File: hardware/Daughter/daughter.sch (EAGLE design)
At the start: 4 parts, among them J1 12V input

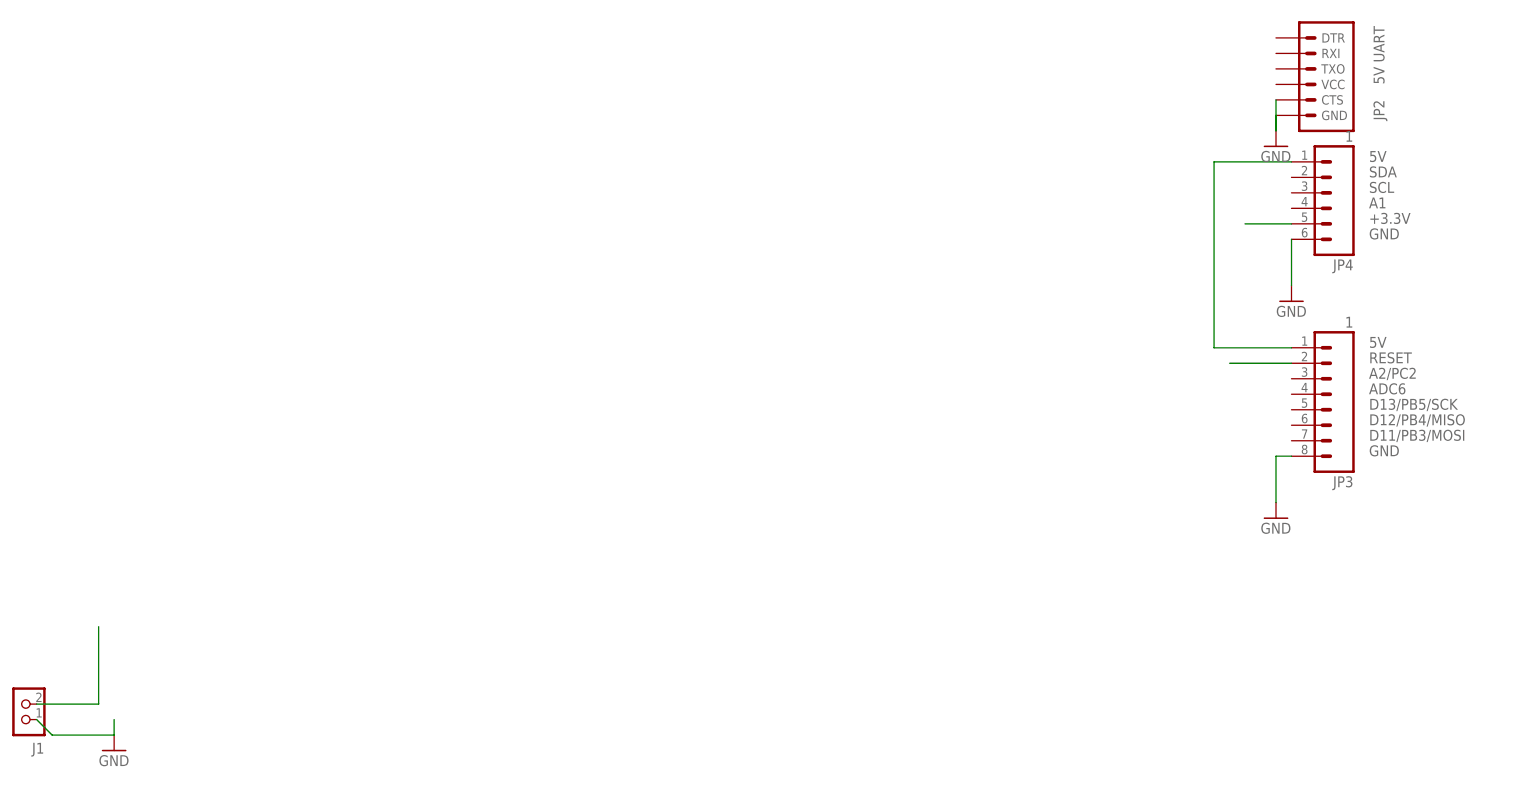
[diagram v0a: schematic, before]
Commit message: added 12_adc_daughter/LTC2495_16x_pga_adc.pdf removed eagle.epf files and added gitignore file
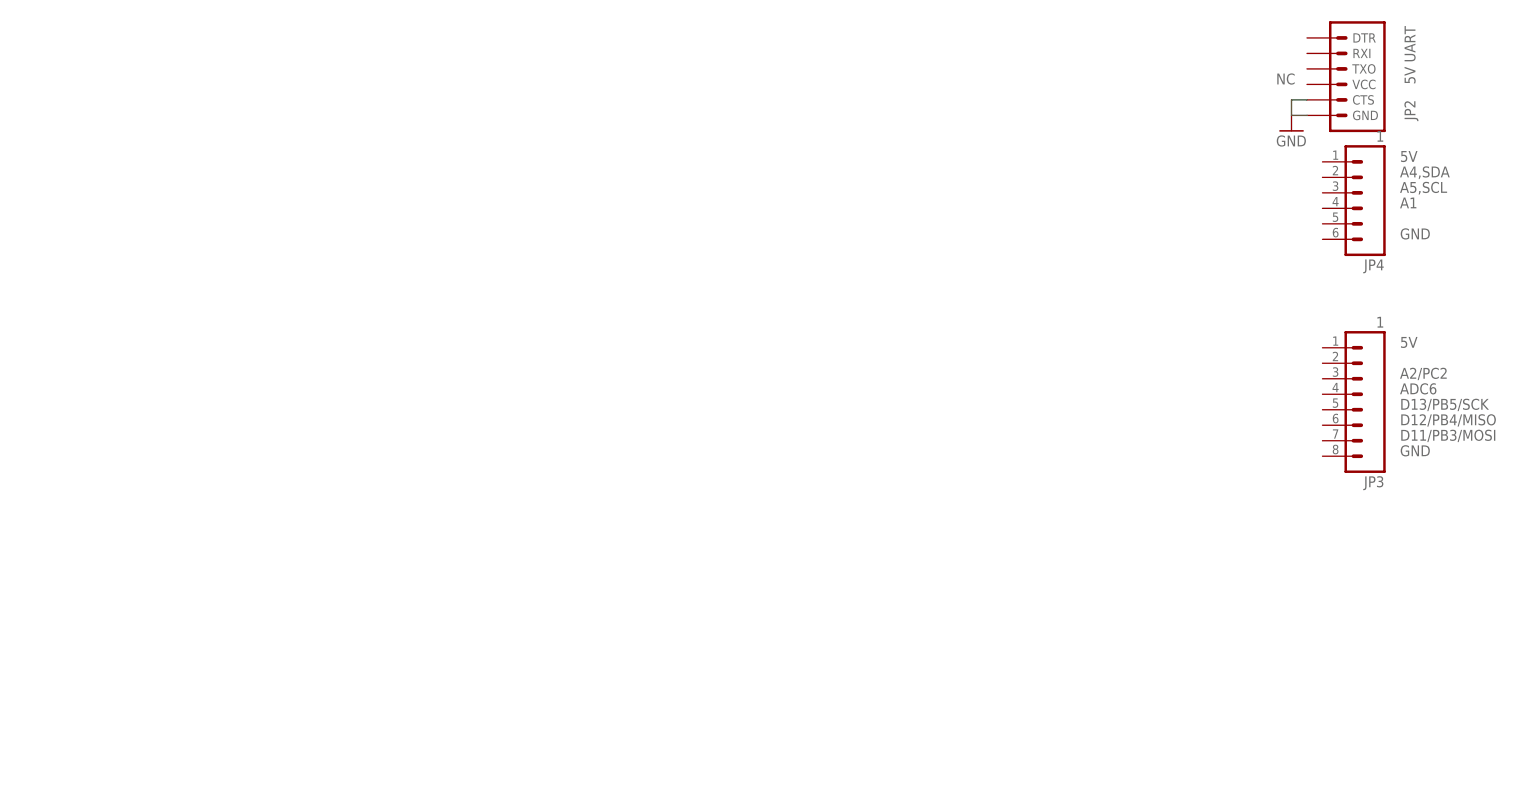
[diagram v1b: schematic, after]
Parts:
- removed J1: 12V input, dp_devices:CON_HEADER_1X02-PTH
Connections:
- removed net +12V: J1.2
- removed net +3.3V: JP4.5
- removed net +5V: JP3.1, JP4.1
- removed net RESET: JP3.2
- net GND: no longer J1.1, JP3.8, JP4.6
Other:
- note added: "A4,SDA"
- note added: "A5,SCL"
- note added: "NC"
- note removed: "SCL"
- note removed: "SDA"
- moved on the sheet: JP2, JP3, JP4
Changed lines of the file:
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@@
 </classes>
 <parts>
-<part name="J1" library="dp_devices" deviceset="CON_HEADER_1X02" device="-PTH" value="12V input"/>
-<part name="GND32" library="SparkFun" deviceset="GND" device=""/>
 <part name="JP2" library="SparkFun" deviceset="ARDUINO_SERIAL_PROGRAM" device="PTH" value="5V UART"/>
 <part name="GND3" library="SparkFun" deviceset="GND" device=""/>
 <part name="JP4" library="SparkFun-Connectors" deviceset="M06" device="SIP" value="1"/>
-<part name="GND5" library="SparkFun" deviceset="GND" device=""/>
-<part name="GND6" library="SparkFun" deviceset="GND" device=""/>
 <part name="JP3" library="SparkFun-Connectors" deviceset="M08" device="1X08" value="1"/>
 </parts>
@@
 <sheet>
 <plain>
-<text x="213.36" y="190.5" size="1.778" layer="95">SDA</text>
-<text x="213.36" y="187.96" size="1.778" layer="95">SCL</text>
-<text x="213.36" y="185.42" size="1.778" layer="95">A1</text>
-<text x="213.36" y="193.04" size="1.778" layer="95">5V</text>
-<text x="213.36" y="162.56" size="1.778" layer="95">5V</text>
-<text x="213.36" y="144.78" size="1.778" layer="95">GND</text>
-<text x="213.36" y="180.34" size="1.778" layer="95">GND</text>
-<text x="213.36" y="157.48" size="1.778" layer="95">A2/PC2</text>
-<text x="213.36" y="154.94" size="1.778" layer="95">ADC6</text>
-<text x="213.36" y="152.4" size="1.778" layer="95">D13/PB5/SCK</text>
-<text x="213.36" y="149.86" size="1.778" layer="95">D12/PB4/MISO</text>
-<text x="213.36" y="147.32" size="1.778" layer="95">D11/PB3/MOSI</text>
+<text x="218.44" y="190.5" size="1.778" layer="95">A4,SDA</text>
+<text x="218.44" y="187.96" size="1.778" layer="95">A5,SCL</text>
+<text x="218.44" y="185.42" size="1.778" layer="95">A1</text>
+<text x="218.44" y="193.04" size="1.778" layer="95">5V</text>
+<text x="218.44" y="162.56" size="1.778" layer="95">5V</text>
+<text x="218.44" y="144.78" size="1.778" layer="95">GND</text>
+<text x="218.44" y="180.34" size="1.778" layer="95">GND</text>
+<text x="218.44" y="157.48" size="1.778" layer="95">A2/PC2</text>
+<text x="218.44" y="154.94" size="1.778" layer="95">ADC6</text>
+<text x="218.44" y="152.4" size="1.778" layer="95">D13/PB5/SCK</text>
+<text x="218.44" y="149.86" size="1.778" layer="95">D12/PB4/MISO</text>
+<text x="218.44" y="147.32" size="1.778" layer="95">D11/PB3/MOSI</text>
+<text x="198.12" y="205.74" size="1.778" layer="96">NC</text>
 </plain>
 <instances>
-<instance part="J1" gate="J" x="-5.08" y="101.6" rot="R180"/>
-<instance part="GND32" gate="1" x="7.62" y="96.52"/>
-<instance part="JP2" gate="G$1" x="203.2" y="208.28" smashed="yes" rot="R180">
-<attribute name="VALUE" x="215.9" y="205.74" size="1.778" layer="96" rot="R90"/>
-<attribute name="NAME" x="214.122" y="203.2" size="1.778" layer="95" rot="R270"/>
+<instance part="JP2" gate="G$1" x="208.28" y="208.28" smashed="yes" rot="R180">
+<attribute name="VALUE" x="220.98" y="205.74" size="1.778" layer="96" rot="R90"/>
+<attribute name="NAME" x="219.202" y="203.2" size="1.778" layer="95" rot="R270"/>
 </instance>
-<instance part="GND3" gate="1" x="198.12" y="195.58"/>
-<instance part="JP4" gate="G$1" x="205.74" y="187.96" rot="R180"/>
-<instance part="GND5" gate="1" x="200.66" y="170.18"/>
-<instance part="GND6" gate="1" x="198.12" y="134.62"/>
-<instance part="JP3" gate="G$1" x="205.74" y="154.94" rot="R180"/>
+<instance part="GND3" gate="1" x="200.66" y="198.12"/>
+<instance part="JP4" gate="G$1" x="210.82" y="187.96" rot="R180"/>
+<instance part="JP3" gate="G$1" x="210.82" y="154.94" rot="R180"/>
 </instances>
 <busses>
@@
 <net name="GND" class="0">
 <segment>
-<wire x1="7.62" y1="99.06" x2="7.62" y2="101.6" width="0.1524" layer="91"/>
-<pinref part="GND32" gate="1" pin="GND"/>
-<wire x1="7.62" y1="99.06" x2="-2.54" y2="99.06" width="0.1524" layer="91"/>
-<wire x1="-2.54" y1="99.06" x2="-5.08" y2="101.6" width="0.1524" layer="91"/>
-<pinref part="J1" gate="J" pin="1"/>
-</segment>
-<segment>
-<wire x1="198.12" y1="203.2" x2="198.12" y2="198.12" width="0.1524" layer="91"/>
-<wire x1="198.12" y1="200.66" x2="198.12" y2="198.12" width="0.1524" layer="91"/>
+<wire x1="203.2" y1="203.2" x2="200.66" y2="203.2" width="0.1524" layer="91"/>
+<wire x1="200.66" y1="203.2" x2="200.66" y2="200.66" width="0.1524" layer="91"/>
+<wire x1="203.2" y1="200.66" x2="200.66" y2="200.66" width="0.1524" layer="91"/>
 <pinref part="JP2" gate="G$1" pin="GND"/>
 <pinref part="GND3" gate="1" pin="GND"/>
 <pinref part="JP2" gate="G$1" pin="CTS"/>
 </segment>
-<segment>
-<pinref part="JP4" gate="G$1" pin="6"/>
-<pinref part="GND5" gate="1" pin="GND"/>
-<wire x1="200.66" y1="180.34" x2="200.66" y2="172.72" width="0.1524" layer="91"/>
-</segment>
-<segment>
-<pinref part="GND6" gate="1" pin="GND"/>
-<wire x1="198.12" y1="144.78" x2="198.12" y2="137.16" width="0.1524" layer="91"/>
-<pinref part="JP3" gate="G$1" pin="8"/>
-<wire x1="200.66" y1="144.78" x2="198.12" y2="144.78" width="0.1524" layer="91"/>
-</segment>
 </net>
-<net name="+5V" class="0">
-<segment>
-<pinref part="JP3" gate="G$1" pin="1"/>
-<wire x1="200.66" y1="162.56" x2="187.96" y2="162.56" width="0.1524" layer="91"/>
-<pinref part="JP4" gate="G$1" pin="1"/>
-<wire x1="200.66" y1="193.04" x2="187.96" y2="193.04" width="0.1524" layer="91"/>
-<wire x1="187.96" y1="193.04" x2="187.96" y2="162.56" width="0.1524" layer="91"/>
-</segment>
-</net>
-<net name="+3.3V" class="0">
-<segment>
-<pinref part="JP4" gate="G$1" pin="5"/>
-<wire x1="200.66" y1="182.88" x2="193.04" y2="182.88" width="0.1524" layer="91"/>
-<label x="213.36" y="182.88" size="1.778" layer="95"/>
-</segment>
-</net>
-<net name="+12V" class="0">
-<segment>
-<pinref part="J1" gate="J" pin="2"/>
-<wire x1="-5.08" y1="104.14" x2="5.08" y2="104.14" width="0.1524" layer="91"/>
-<wire x1="5.08" y1="104.14" x2="5.08" y2="116.84" width="0.1524" layer="91"/>
-</segment>
-</net>
-<net name="RESET" class="0">
-<segment>
-<pinref part="JP3" gate="G$1" pin="2"/>
-<wire x1="200.66" y1="160.02" x2="190.5" y2="160.02" width="0.1524" layer="91"/>
-<label x="213.36" y="160.02" size="1.778" layer="95"/>
-</segment>
-</net>
